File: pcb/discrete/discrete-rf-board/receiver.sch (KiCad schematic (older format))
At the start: 31 parts, among them U7 MAX1193

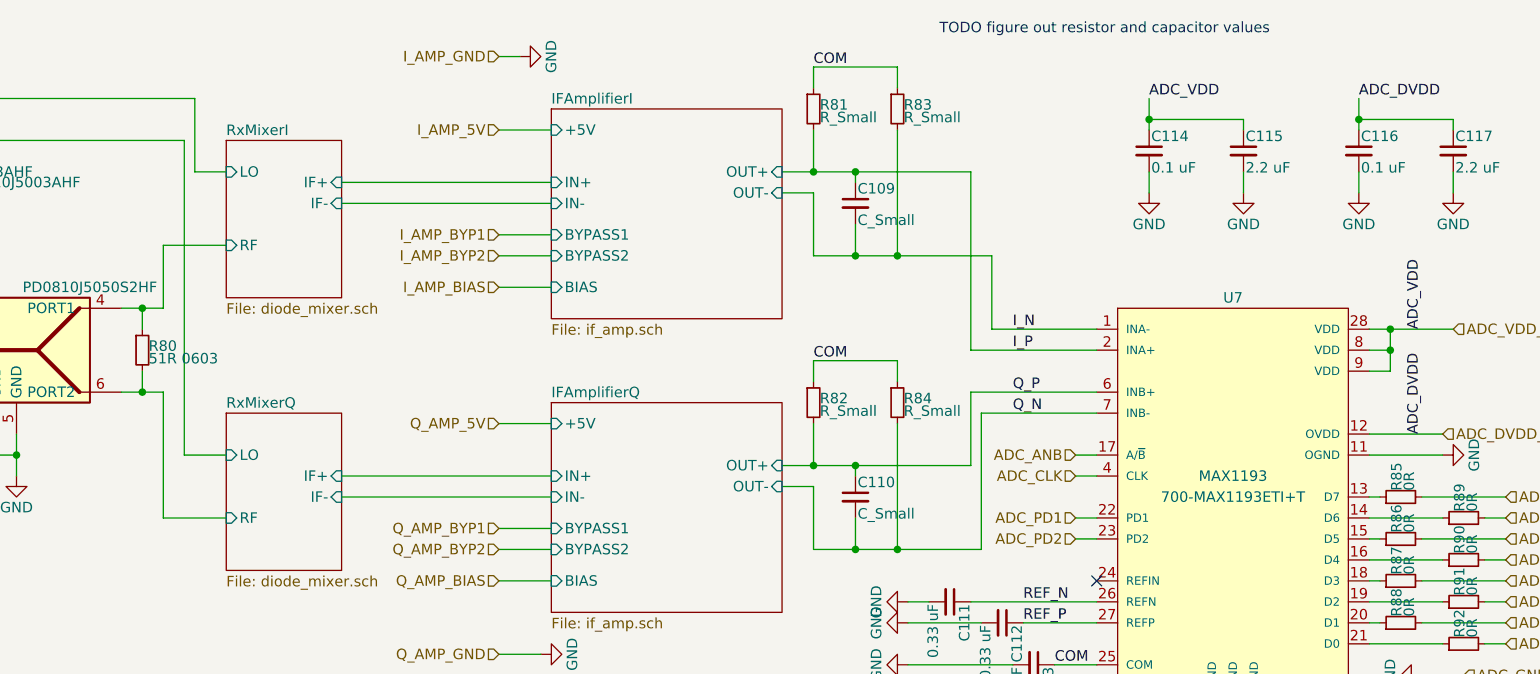
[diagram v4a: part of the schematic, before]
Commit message: All component values set (TODO change transistor gain stages to match values from experimentation
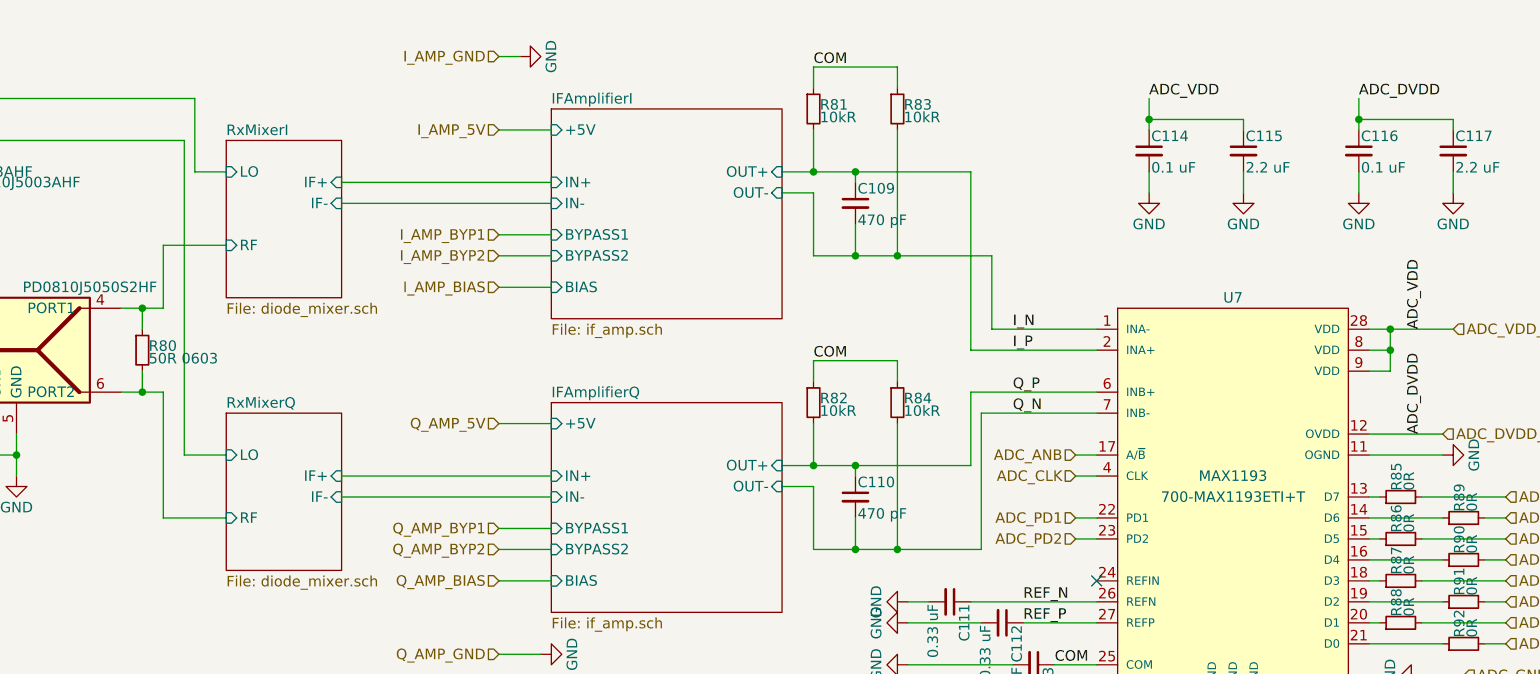
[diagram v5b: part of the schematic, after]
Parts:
- C109, C110: value C_Small -> 470 pF
- FL4: footprint (none) -> discrete_footprints:Murata_SM2016-4
- R80: value 51R 0603 -> 50R 0603
- R81, R82, R83, R84: value R_Small -> 10kR
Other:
- note removed: "TODO figure out resistor and capacitor values"
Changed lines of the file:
@@
 F 0 "FL4" H 2500 3900 50  0000 C CNN
 F 1 "SF2098H" H 3000 3900 50  0000 C CNN
-F 2 "" H 2750 3150 50  0001 C CNN
+F 2 "discrete_footprints:Murata_SM2016-4" H 2750 3150 50  0001 C CNN
 F 3 "" H 2750 4000 50  0001 C CNN
 F 4 "719-SF2098H " H 2750 3600 50  0001 C CNN "Mouser"
@@
 P 7550 3850
 F 0 "R82" H 7580 3870 50  0000 L CNN
-F 1 "R_Small" H 7580 3810 50  0000 L CNN
+F 1 "10kR" H 7580 3810 50  0000 L CNN
 F 2 "" H 7550 3850 50  0001 C CNN
 F 3 "~" H 7550 3850 50  0001 C CNN
@@
 P 7950 3850
 F 0 "R84" H 7980 3870 50  0000 L CNN
-F 1 "R_Small" H 7980 3810 50  0000 L CNN
+F 1 "10kR" H 7980 3810 50  0000 L CNN
 F 2 "" H 7950 3850 50  0001 C CNN
 F 3 "~" H 7950 3850 50  0001 C CNN
@@
 P 7750 4300
 F 0 "C110" H 7760 4370 50  0000 L CNN
-F 1 "C_Small" H 7760 4220 50  0000 L CNN
+F 1 "470 pF" H 7760 4220 50  0000 L CNN
 F 2 "" H 7750 4300 50  0001 C CNN
 F 3 "~" H 7750 4300 50  0001 C CNN
@@
 P 7550 2450
 F 0 "R81" H 7580 2470 50  0000 L CNN
-F 1 "R_Small" H 7580 2410 50  0000 L CNN
+F 1 "10kR" H 7580 2410 50  0000 L CNN
 F 2 "" H 7550 2450 50  0001 C CNN
 F 3 "~" H 7550 2450 50  0001 C CNN
@@
 P 7950 2450
 F 0 "R83" H 7980 2470 50  0000 L CNN
-F 1 "R_Small" H 7980 2410 50  0000 L CNN
+F 1 "10kR" H 7980 2410 50  0000 L CNN
 F 2 "" H 7950 2450 50  0001 C CNN
 F 3 "~" H 7950 2450 50  0001 C CNN
@@
 P 7750 2900
 F 0 "C109" H 7760 2970 50  0000 L CNN
-F 1 "C_Small" H 7760 2820 50  0000 L CNN
+F 1 "470 pF" H 7760 2820 50  0000 L CNN
 F 2 "" H 7750 2900 50  0001 C CNN
 F 3 "~" H 7750 2900 50  0001 C CNN
@@
 Text Label 8550 4900 0    50   ~ 0
 REF_P
-Text Notes 8150 2100 0    50   ~ 0
-TODO figure out resistor and capacitor values
 Text Label 9150 2400 0    50   ~ 0
 ADC_VDD
@@
 P 4350 3600
 F 0 "R80" H 4380 3620 50  0000 L CNN
-F 1 "51R 0603" H 4380 3560 50  0000 L CNN
+F 1 "50R 0603" H 4380 3560 50  0000 L CNN
 F 2 "" H 4350 3600 50  0001 C CNN
 F 3 "~" H 4350 3600 50  0001 C CNN

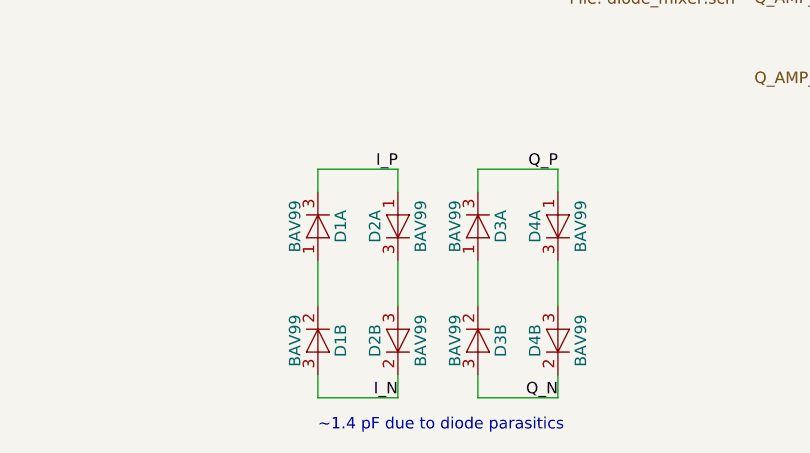
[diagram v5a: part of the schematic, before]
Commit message: Autofill; lots left to do
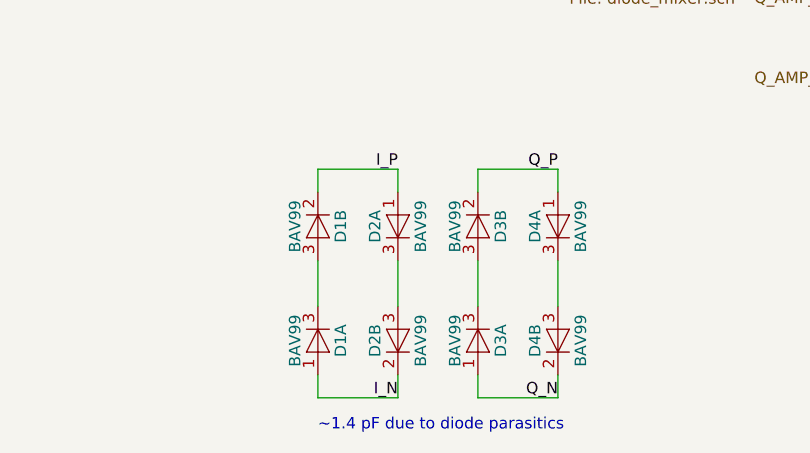
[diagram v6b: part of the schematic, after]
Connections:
- net I_N: now also D1.1 (A); no longer D1.3 (A)
- net I_P: now also D1.2 (K); no longer D1.3 (K)
- net Q_N: now also D3.1 (A); no longer D3.3 (A)
- net Q_P: now also D3.2 (K); no longer D3.3 (K)
- new net: D1.3 (A), D1.3 (K)
- new net: D3.3 (A), D3.3 (K)
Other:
- moved on the sheet: D1A, D1B, D3A, D3B
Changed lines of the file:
@@
 L Diode:BAV99 D1
 U 2 1 5DD008E8
+P 3650 5700
+F 0 "D1" H 3650 5800 50  0000 C CNN
+F 1 "BAV99" H 3650 5600 50  0000 C CNN
+F 2 "Package_TO_SOT_SMD:SOT-23" H 3650 5550 50  0001 C CNN
+F 3 "https://assets.nexperia.com/documents/data-sheet/BAV99_SER.pdf" H 3650 5800 50  0001 C CNN
+	2    3650 5700
+	0    1    1    0
+$EndComp
+$Comp
+L Diode:BAV99 D1
+U 1 1 5DD008EE
 P 3650 6200
 F 0 "D1" H 3650 6300 50  0000 C CNN
@@
 F 2 "Package_TO_SOT_SMD:SOT-23" H 3650 6050 50  0001 C CNN
 F 3 "https://assets.nexperia.com/documents/data-sheet/BAV99_SER.pdf" H 3650 6300 50  0001 C CNN
-	2    3650 6200
-	0    1    1    0
-$EndComp
-$Comp
-L Diode:BAV99 D1
-U 1 1 5DD008EE
-P 3650 5700
-F 0 "D1" H 3650 5800 50  0000 C CNN
-F 1 "BAV99" H 3650 5600 50  0000 C CNN
-F 2 "Package_TO_SOT_SMD:SOT-23" H 3650 5550 50  0001 C CNN
-F 3 "https://assets.nexperia.com/documents/data-sheet/BAV99_SER.pdf" H 3650 5800 50  0001 C CNN
-	1    3650 5700
+	1    3650 6200
 	0    1    1    0
 $EndComp
@@
 L Diode:BAV99 D3
 U 2 1 5DD2A865
+P 4350 5700
+F 0 "D3" H 4350 5800 50  0000 C CNN
+F 1 "BAV99" H 4350 5600 50  0000 C CNN
+F 2 "Package_TO_SOT_SMD:SOT-23" H 4350 5550 50  0001 C CNN
+F 3 "https://assets.nexperia.com/documents/data-sheet/BAV99_SER.pdf" H 4350 5800 50  0001 C CNN
+	2    4350 5700
+	0    1    1    0
+$EndComp
+$Comp
+L Diode:BAV99 D3
+U 1 1 5DD2A86B
 P 4350 6200
 F 0 "D3" H 4350 6300 50  0000 C CNN
@@
 F 2 "Package_TO_SOT_SMD:SOT-23" H 4350 6050 50  0001 C CNN
 F 3 "https://assets.nexperia.com/documents/data-sheet/BAV99_SER.pdf" H 4350 6300 50  0001 C CNN
-	2    4350 6200
+	1    4350 6200
 	0    1    1    0
 $EndComp
-$Comp
-L Diode:BAV99 D3
-U 1 1 5DD2A86B
-P 4350 5700
-F 0 "D3" H 4350 5800 50  0000 C CNN
-F 1 "BAV99" H 4350 5600 50  0000 C CNN
-F 2 "Package_TO_SOT_SMD:SOT-23" H 4350 5550 50  0001 C CNN
-F 3 "https://assets.nexperia.com/documents/data-sheet/BAV99_SER.pdf" H 4350 5800 50  0001 C CNN
-	1    4350 5700
-	0    1    1    0
-$EndComp

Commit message: Footprint some stuff
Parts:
- C113: footprint (none) -> Capacitor_SMD:C_0603_1608Metric_Pad1.05x0.95mm_HandSolder; Mouser (none) -> 710-885012106014
- D1: Mouser (none) -> 863-BAV99RWT1G
- U7: footprint (none) -> discrete_footprints:Maxim_TQFN28-EP
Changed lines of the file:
@@
 F 0 "U7" H 9550 3450 50  0000 C CNN
 F 1 "MAX1193" H 9550 2600 50  0000 C CNN
-F 2 "" H 9550 3400 50  0001 C CNN
+F 2 "discrete_footprints:Maxim_TQFN28-EP" H 9550 3400 50  0001 C CNN
 F 3 "" H 9550 3400 50  0001 C CNN
 F 4 " 700-MAX1193ETI+T " H 9550 2500 50  0000 C CNN "Mouser"
@@
 F 0 "C113" H 8610 5170 50  0000 L CNN
 F 1 "0.33 uF" H 8610 5020 50  0000 L CNN
-F 2 "" H 8600 5100 50  0001 C CNN
+F 2 "Capacitor_SMD:C_0603_1608Metric_Pad1.05x0.95mm_HandSolder" H 8600 5100 50  0001 C CNN
 F 3 "~" H 8600 5100 50  0001 C CNN
+F 4 "710-885012106014" H 8600 5100 50  0001 C CNN "Mouser"
 	1    8600 5100
 	0    1    1    0
@@
 F 2 "Package_TO_SOT_SMD:SOT-23" H 3650 5550 50  0001 C CNN
 F 3 "https://assets.nexperia.com/documents/data-sheet/BAV99_SER.pdf" H 3650 5800 50  0001 C CNN
+F 4 " 863-BAV99RWT1G" H 3650 5700 50  0001 C CNN "Mouser"
 	2    3650 5700
 	0    1    1    0

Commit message: Autofill
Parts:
- C111, C112: footprint (none) -> Capacitor_SMD:C_0603_1608Metric_Pad1.05x0.95mm_HandSolder; Mouser (none) -> 710-885012106014
- D1, D2, D3, D4: Mouser (none) -> 863-BAV99RWT1G
- R85, R86, R87, R88, R89, R90, R91, R92: footprint (none) -> Capacitor_SMD:C_0402_1005Metric; Mouser (none) -> 71-CRCW04020000Z0EDC
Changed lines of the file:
@@
 F 0 "C111" H 8210 4870 50  0000 L CNN
 F 1 "0.33 uF" H 8210 4720 50  0000 L CNN
-F 2 "" H 8200 4800 50  0001 C CNN
+F 2 "Capacitor_SMD:C_0603_1608Metric_Pad1.05x0.95mm_HandSolder" H 8200 4800 50  0001 C CNN
 F 3 "~" H 8200 4800 50  0001 C CNN
+F 4 "710-885012106014" H 8200 4800 50  0001 C CNN "Mouser"
 	1    8200 4800
 	0    1    1    0
@@
 F 0 "C112" H 8460 4970 50  0000 L CNN
 F 1 "0.33 uF" H 8460 4820 50  0000 L CNN
-F 2 "" H 8450 4900 50  0001 C CNN
+F 2 "Capacitor_SMD:C_0603_1608Metric_Pad1.05x0.95mm_HandSolder" H 8450 4900 50  0001 C CNN
 F 3 "~" H 8450 4900 50  0001 C CNN
+F 4 "710-885012106014" H 8450 4900 50  0001 C CNN "Mouser"
 	1    8450 4900
 	0    1    1    0
@@
 F 0 "R85" H 10380 4320 50  0000 L CNN
 F 1 "0R" H 10380 4260 50  0000 L CNN
-F 2 "" H 10350 4300 50  0001 C CNN
+F 2 "Capacitor_SMD:C_0402_1005Metric" H 10350 4300 50  0001 C CNN
 F 3 "~" H 10350 4300 50  0001 C CNN
+F 4 "71-CRCW04020000Z0EDC" H 10350 4300 50  0001 C CNN "Mouser"
 	1    10350 4300
 	0    -1   -1   0
@@
 F 0 "R89" H 10680 4420 50  0000 L CNN
 F 1 "0R" H 10680 4360 50  0000 L CNN
-F 2 "" H 10650 4400 50  0001 C CNN
+F 2 "Capacitor_SMD:C_0402_1005Metric" H 10650 4400 50  0001 C CNN
 F 3 "~" H 10650 4400 50  0001 C CNN
+F 4 "71-CRCW04020000Z0EDC" H 10650 4400 50  0001 C CNN "Mouser"
 	1    10650 4400
 	0    -1   -1   0
@@
 F 0 "R86" H 10380 4520 50  0000 L CNN
 F 1 "0R" H 10380 4460 50  0000 L CNN
-F 2 "" H 10350 4500 50  0001 C CNN
+F 2 "Capacitor_SMD:C_0402_1005Metric" H 10350 4500 50  0001 C CNN
 F 3 "~" H 10350 4500 50  0001 C CNN
+F 4 "71-CRCW04020000Z0EDC" H 10350 4500 50  0001 C CNN "Mouser"
 	1    10350 4500
 	0    -1   -1   0
@@
 F 0 "R90" H 10680 4620 50  0000 L CNN
 F 1 "0R" H 10680 4560 50  0000 L CNN
-F 2 "" H 10650 4600 50  0001 C CNN
+F 2 "Capacitor_SMD:C_0402_1005Metric" H 10650 4600 50  0001 C CNN
 F 3 "~" H 10650 4600 50  0001 C CNN
+F 4 "71-CRCW04020000Z0EDC" H 10650 4600 50  0001 C CNN "Mouser"
 	1    10650 4600
 	0    -1   -1   0
@@
 F 0 "R87" H 10380 4720 50  0000 L CNN
 F 1 "0R" H 10380 4660 50  0000 L CNN
-F 2 "" H 10350 4700 50  0001 C CNN
+F 2 "Capacitor_SMD:C_0402_1005Metric" H 10350 4700 50  0001 C CNN
 F 3 "~" H 10350 4700 50  0001 C CNN
+F 4 "71-CRCW04020000Z0EDC" H 10350 4700 50  0001 C CNN "Mouser"
 	1    10350 4700
 	0    -1   -1   0
@@
 F 0 "R91" H 10680 4820 50  0000 L CNN
 F 1 "0R" H 10680 4760 50  0000 L CNN
-F 2 "" H 10650 4800 50  0001 C CNN
+F 2 "Capacitor_SMD:C_0402_1005Metric" H 10650 4800 50  0001 C CNN
 F 3 "~" H 10650 4800 50  0001 C CNN
+F 4 "71-CRCW04020000Z0EDC" H 10650 4800 50  0001 C CNN "Mouser"
 	1    10650 4800
 	0    -1   -1   0
@@
 F 0 "R88" H 10380 4920 50  0000 L CNN
 F 1 "0R" H 10380 4860 50  0000 L CNN
-F 2 "" H 10350 4900 50  0001 C CNN
+F 2 "Capacitor_SMD:C_0402_1005Metric" H 10350 4900 50  0001 C CNN
 F 3 "~" H 10350 4900 50  0001 C CNN
+F 4 "71-CRCW04020000Z0EDC" H 10350 4900 50  0001 C CNN "Mouser"
 	1    10350 4900
 	0    -1   -1   0
@@
 F 0 "R92" H 10680 5020 50  0000 L CNN
 F 1 "0R" H 10680 4960 50  0000 L CNN
-F 2 "" H 10650 5000 50  0001 C CNN
+F 2 "Capacitor_SMD:C_0402_1005Metric" H 10650 5000 50  0001 C CNN
 F 3 "~" H 10650 5000 50  0001 C CNN
+F 4 "71-CRCW04020000Z0EDC" H 10650 5000 50  0001 C CNN "Mouser"
 	1    10650 5000
 	0    -1   -1   0
@@
 F 2 "Package_TO_SOT_SMD:SOT-23" H 3650 6050 50  0001 C CNN
 F 3 "https://assets.nexperia.com/documents/data-sheet/BAV99_SER.pdf" H 3650 6300 50  0001 C CNN
+F 4 " 863-BAV99RWT1G" H 3650 6300 50  0001 C CNN "Mouser"
 	1    3650 6200
 	0    1    1    0
@@
 F 2 "Package_TO_SOT_SMD:SOT-23" H 4000 5550 50  0001 C CNN
 F 3 "https://assets.nexperia.com/documents/data-sheet/BAV99_SER.pdf" H 4000 5800 50  0001 C CNN
+F 4 " 863-BAV99RWT1G" H 4000 5800 50  0001 C CNN "Mouser"
 	1    4000 5700
 	0    -1   -1   0
@@
 F 2 "Package_TO_SOT_SMD:SOT-23" H 4000 6050 50  0001 C CNN
 F 3 "https://assets.nexperia.com/documents/data-sheet/BAV99_SER.pdf" H 4000 6300 50  0001 C CNN
+F 4 " 863-BAV99RWT1G" H 4000 6300 50  0001 C CNN "Mouser"
 	2    4000 6200
 	0    -1   -1   0
@@
 F 2 "Package_TO_SOT_SMD:SOT-23" H 4350 5550 50  0001 C CNN
 F 3 "https://assets.nexperia.com/documents/data-sheet/BAV99_SER.pdf" H 4350 5800 50  0001 C CNN
+F 4 " 863-BAV99RWT1G" H 4350 5800 50  0001 C CNN "Mouser"
 	2    4350 5700
 	0    1    1    0
@@
 F 2 "Package_TO_SOT_SMD:SOT-23" H 4350 6050 50  0001 C CNN
 F 3 "https://assets.nexperia.com/documents/data-sheet/BAV99_SER.pdf" H 4350 6300 50  0001 C CNN
+F 4 " 863-BAV99RWT1G" H 4350 6300 50  0001 C CNN "Mouser"
 	1    4350 6200
 	0    1    1    0
@@
 F 2 "Package_TO_SOT_SMD:SOT-23" H 4700 6050 50  0001 C CNN
 F 3 "https://assets.nexperia.com/documents/data-sheet/BAV99_SER.pdf" H 4700 6300 50  0001 C CNN
+F 4 " 863-BAV99RWT1G" H 4700 6300 50  0001 C CNN "Mouser"
 	2    4700 6200
 	0    -1   -1   0
@@
 F 2 "Package_TO_SOT_SMD:SOT-23" H 4700 5550 50  0001 C CNN
 F 3 "https://assets.nexperia.com/documents/data-sheet/BAV99_SER.pdf" H 4700 5800 50  0001 C CNN
+F 4 " 863-BAV99RWT1G" H 4700 5800 50  0001 C CNN "Mouser"
 	1    4700 5700
 	0    -1   -1   0
